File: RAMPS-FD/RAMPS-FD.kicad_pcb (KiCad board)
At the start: 2 copper layers, 100 x 100 mm, 171 parts, among them J1 NET-TIE, K201 S1, K202 S2, K203 S3, K204 S4, M101 LOGO_OSHW, P1 SERIAL1, P101 HB_IN, P102 RESET, P105 12V-AUX, P107 MOT_IN, P108 POWER_IN, P2 I2C-1, P201 3 2 1, P202 3 2 1, P203 3 2 1, P204 X, P205 Y, P206 Z1, P207 3 2 1, P208 3 2 1, P209 3 2 1, P210 E2, P211 I2C-0, P212 E1, P213 AUX-4, P214 AUX-2, P215 AUX-3, P216 SERIAL0, P217 E0, P218 D11, P219 EXT_5V, P3 Z2, P301 THERMISTORS, P302 ESTOP, P403 D9, P404 D8, P405 D10, P801 ENDSTOPS, P802 - X + - Y + - Z +, P901 D12, P902 D2, Q1 DMN2075, Q101 DMN2075, Q201 IRLB8743PBF, Q202 IRLB8743PBF, Q203 IRLB8743PBF, Q206 IRLB8743PBF, Q901 DMN2075U, Q902 DMN2075U, SW101 RESET, U1 74ACT125, U1001 TL431_SOT23_RMC, U2 74ACT244, U201 X, U202 Y, U203 Z, U204 E2, U205 E1, U206 E0, U3 LM7812, U4 L7805CV-DG, U601 24C512, U801 4050_RMC

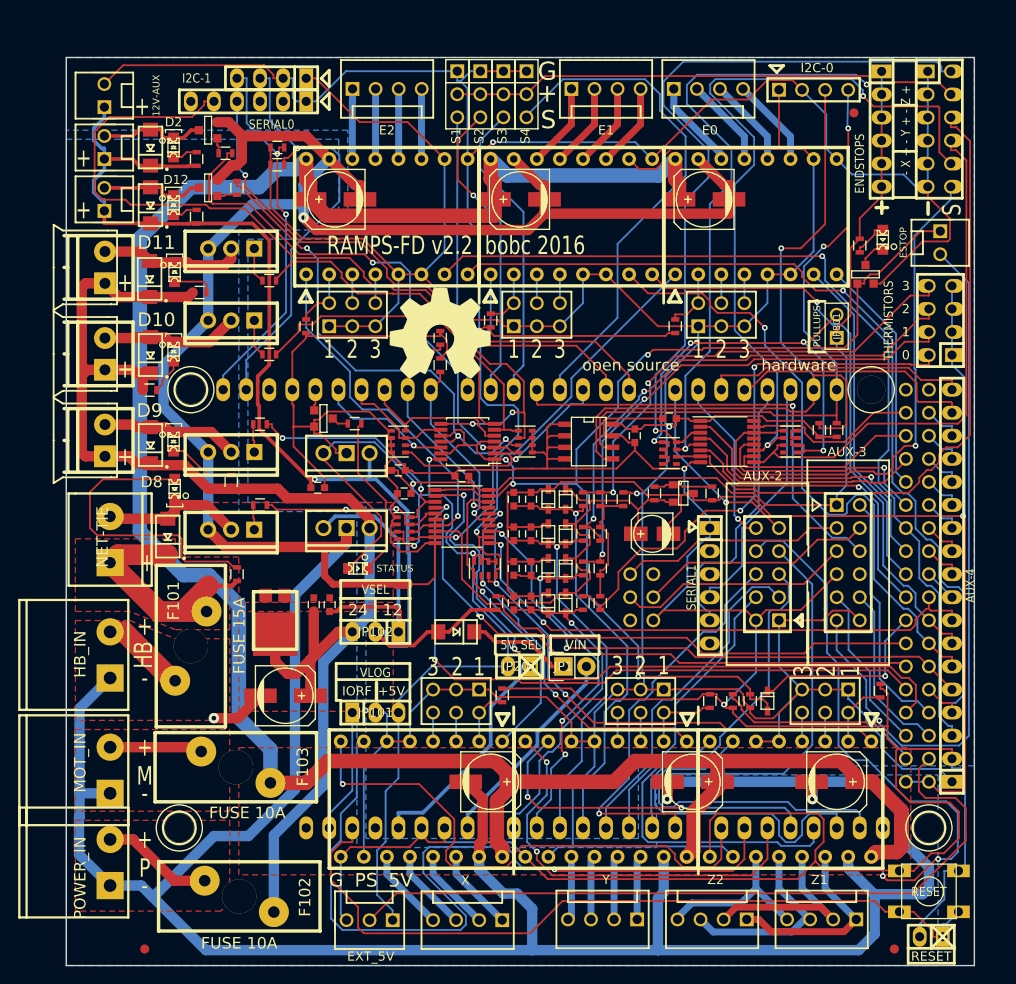
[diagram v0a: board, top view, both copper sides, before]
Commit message: Changed fuse holders to Keystone 3568; specificy HCT instead of ACT logic
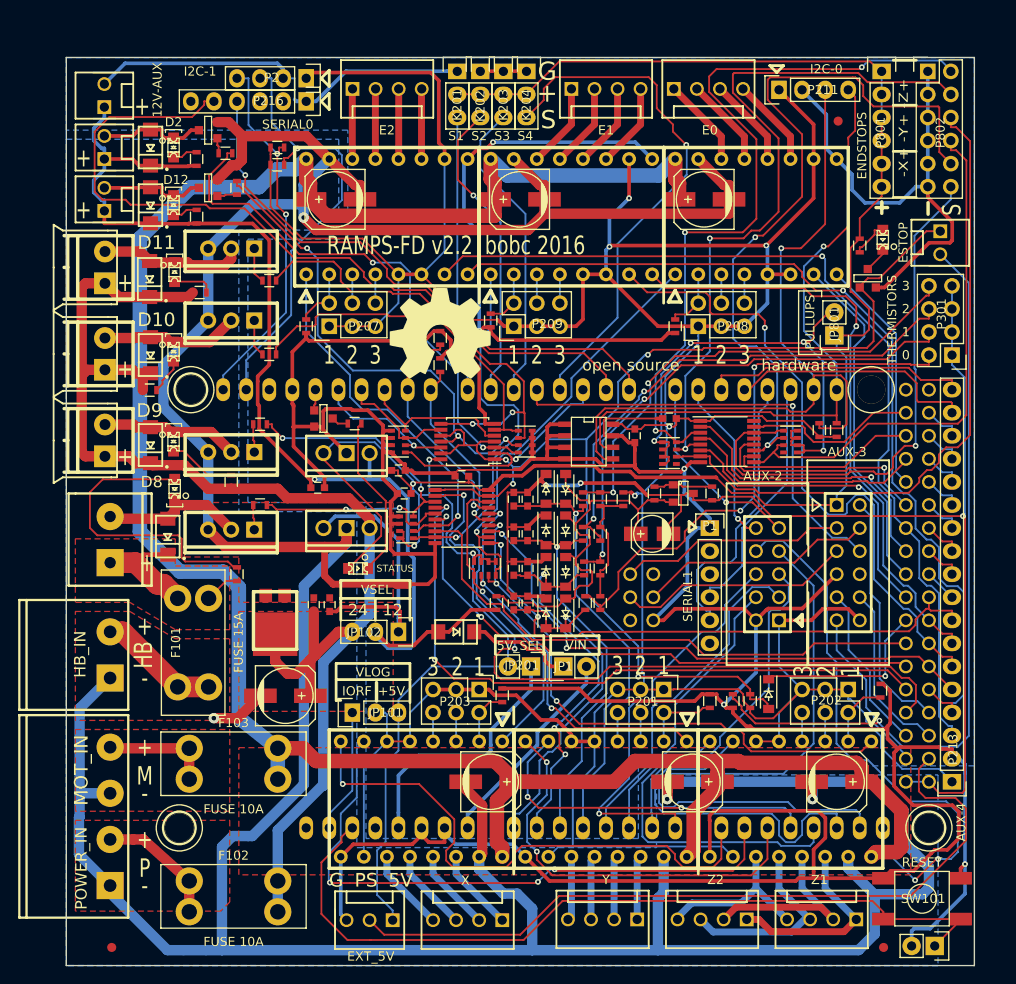
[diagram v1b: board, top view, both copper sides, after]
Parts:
- removed P107: MOT_IN, w_conn_screw:mstba_2,5%2f2-g-5,08
- C101: value 100u 35V -> 100u; 35V
- C102: value 100n 35V -> 100n; 50V
- C207, C3: value 100n 16V -> 100n
- D1001, D1002, D1003, D1004, D1005, D1006, D1007, D1008, D301: footprint w_smd_diode:SOD323 -> Diodes_SMD:SOD-123
- D102: value SS10Pxx -> V10P10
- F101, F102, F103: footprint rmc:FUSE-MINI-AUTO -> rmc:Keystone_3568
- JP101, JP102: footprint w_pin_strip:pin_strip_3 -> Pin_Headers:Pin_Header_Straight_1x03
- JP201, P102: footprint w_pin_strip:pin_strip_2 -> Pin_Headers:Pin_Header_Straight_1x02
- JP801: footprint pin_array:PIN_ARRAY_2X1 -> Pin_Headers:Pin_Header_Straight_1x02
- K201, K202, K203, K204: footprint pin_array:PIN_ARRAY_3X1 -> Pin_Headers:Pin_Header_Straight_1x03
- P1, P216, P801: footprint w_pin_strip:pin_strip_6 -> Pin_Headers:Pin_Header_Straight_1x06
- P108: footprint w_conn_screw:mstba_2,5%2f2-g-5,08 -> w_conn_screw:mstba_2,5%2f4-g-5,08
- P2: footprint w_pin_strip:pin_strip_4 -> Pin_Headers:Pin_Header_Straight_1x04
- P201, P202, P203, P207, P208, P209: footprint pin_array:pin_array_3x2 -> Pin_Headers:Pin_Header_Straight_2x03
- P211: footprint pin_array:PIN_ARRAY_4x1 -> Pin_Headers:Pin_Header_Straight_1x04
- P213: footprint w_pin_strip:pin_strip_18 -> Pin_Headers:Pin_Header_Straight_1x18
- P301: footprint w_pin_strip:pin_strip_4x2 -> Pin_Headers:Pin_Header_Straight_2x04
- P802: value - X + - Y + - Z + -> -X+ -Y+ -Z+; footprint w_pin_strip:pin_strip_6x2 -> Pin_Headers:Pin_Header_Straight_2x06
- SW101: footprint rmc:SW_6x6_MULTI -> rmc:SW_6x6_SMD
- U1: value 74ACT125 -> 74HCT125
- U2: value 74ACT244 -> 74HCT244
- U801: value 4050_RMC -> 74HC4050
- moved P213 21.6 mm to (149.9, 119.4), turned to 180 degrees
- moved P802 6.48 mm to (147.2, 41.1), turned to 0 degrees
- moved P1 6.35 mm to (123.2, 91.4), turned to 0 degrees
- moved P216 6.35 mm to (78.7, 44.5), turned to 270 degrees
- moved P801 6.35 mm to (142.1, 41.1), turned to 0 degrees
- moved P108 5.08 mm to (57.1, 123.2)
- moved P301 4.02 mm to (149.9, 72.4), turned to 180 degrees
- moved P211 3.81 mm to (130.8, 43.2), turned to 90 degrees
- moved P2 3.81 mm to (78.7, 41.9), turned to 270 degrees
- moved FID1 3.64 mm to (57.3, 137.6)
- moved P202 2.84 mm to (138.4, 109.2), turned to 270 degrees
- moved P209 2.84 mm to (101.6, 69.2), turned to 90 degrees
- moved P201 2.84 mm to (118.1, 109.2), turned to 270 degrees
- moved P203 2.84 mm to (97.8, 109.2), turned to 270 degrees
- moved P207 2.84 mm to (81.3, 69.2), turned to 90 degrees
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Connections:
- D103 pad 1: +12P -> /Power/LP_1
- D103 pad 2: /Power/LP_1 -> +12P
- D301 pad 1: Net-(D301-Pad1) -> ESTOP
- D301 pad 2: ESTOP -> Net-(D301-Pad2)
- D401 pad 1: /Mosfet Outputs/D9_OUT -> +V_POWER
- D401 pad 2: +V_POWER -> /Mosfet Outputs/D9_OUT
- D402 pad 1: /Mosfet Outputs/D10_OUT -> +V_POWER
- D402 pad 2: +V_POWER -> /Mosfet Outputs/D10_OUT
- D403 pad 1: /Mosfet Outputs/FET4_OUT -> +V_POWER
- D403 pad 2: +V_POWER -> /Mosfet Outputs/FET4_OUT
- D404 pad 1: /Mosfet Outputs/D8_OUT -> +V_HEATBED
- D404 pad 2: +V_HEATBED -> /Mosfet Outputs/D8_OUT
- D903 pad 1: /Extra MOSFETs/P_FET5 -> +12P
- D903 pad 2: +12P -> /Extra MOSFETs/P_FET5
- D904 pad 1: /Extra MOSFETs/P_FET6 -> +12P
- D904 pad 2: +12P -> /Extra MOSFETs/P_FET6
- P302 pad 1: Net-(D301-Pad1) -> Net-(D301-Pad2)
- Q1 pad G: Net-(D301-Pad1) -> Net-(D301-Pad2)
- R304 pad 2: Net-(D301-Pad1) -> Net-(D301-Pad2)
- U1 pad 1: Net-(D301-Pad1) -> Net-(D301-Pad2)
- U1 pad 10: Net-(D301-Pad1) -> Net-(D301-Pad2)
- U1 pad 13: Net-(D301-Pad1) -> Net-(D301-Pad2)
- U1 pad 4: Net-(D301-Pad1) -> Net-(D301-Pad2)
- U2 pad 1: Net-(D301-Pad1) -> Net-(D301-Pad2)
- U2 pad 19: Net-(D301-Pad1) -> Net-(D301-Pad2)
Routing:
- net Net-(D301-Pad2): track 0.00 -> 138.3 mm, vias 0 -> 4
- net Net-(D301-Pad1): track 134.4 -> 0.00 mm, vias 4 -> 0
- net GND: track 626.7 -> 605.7 mm, vias 5 -> 6
- net X_STEP: track 87.5 -> 67.5 mm, vias 1 -> 3
- net +V_LOGIC: track 403.1 -> 421.5 mm, vias 2 -> 5
- net +5V: track 268.1 -> 273.2 mm
- net THERM1: track 41.4 -> 45.7 mm
- net /RESET: track 85.7 -> 89.8 mm
- net X_EN: track 77.0 -> 81.0 mm
- net /Power/HB_IN: track 9.39 -> 13.4 mm
- net +V_HEATBED: track 26.9 -> 23.1 mm
- net OV_REF: track 42.2 -> 45.6 mm
- net THERM0: track 37.9 -> 41.3 mm
- net /Z_EN_BUF: track 60.8 -> 63.3 mm
- net D39: track 61.0 -> 63.3 mm
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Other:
- net class Default: clearance 0.2032 -> 0.1778
- net class low-power: clearance 0.2032 -> 0.1778
- rule trace_clearance: 0.2032 -> 0.1778
- board text added: "MOT_IN"

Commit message: Fix 3d view; remove faulty ADC protection
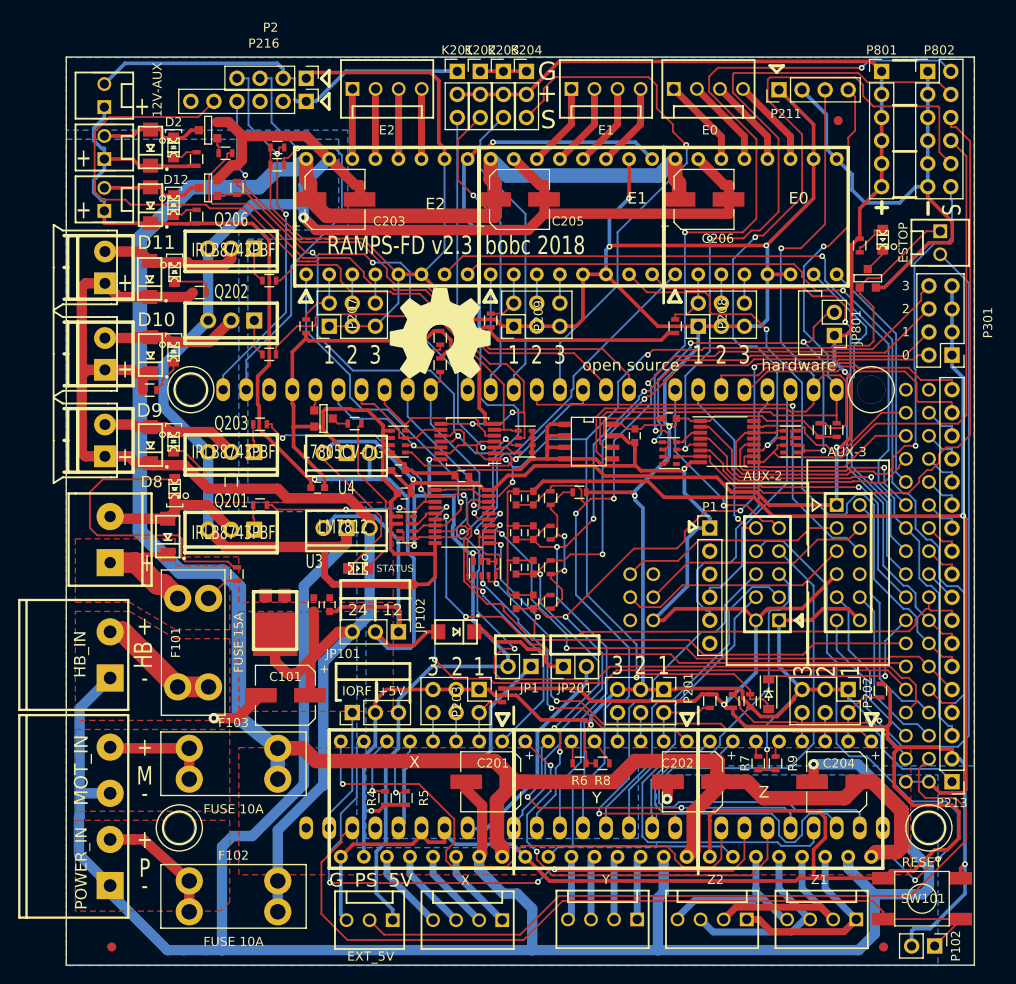
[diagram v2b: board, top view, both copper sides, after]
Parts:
- removed C1001: 10u, Capacitors_SMD:c_elec_4x5.3
- removed D1001, D1002, D1003, D1004, D1005, D1006, D1007, D1008: 1N4148, Diodes_SMD:SOD-123
- removed R1002: 6k8, Resistors_SMD:R_0603
- removed R1003: 1k8, Resistors_SMD:R_0603
- removed R1004: 1k, Resistors_SMD:R_0603
- removed R502, R503, R504, R505: 4k7, Resistors_SMD:R_0603
- removed U1001: TL431_SOT23_RMC, libcms:SOT23
- added R4: 10k, Resistors_SMD:R_0603, F.Cu at (87.4, 121.2)
- added R5: 10k, Resistors_SMD:R_0603, F.Cu at (89.7, 121.2)
- added R6: 10k, Resistors_SMD:R_0603, F.Cu at (108.8, 117.3)
- added R7: 10k, Resistors_SMD:R_0603, F.Cu at (128.5, 117.3)
- added R8: 10k, Resistors_SMD:R_0603, F.Cu at (111.4, 117.3)
- added R9: 10k, Resistors_SMD:R_0603, F.Cu at (130.4, 117.3)
- C101: value 100u; 35V -> 100u 35V; footprint Capacitors_SMD:c_elec_6.3x7.7 -> Capacitors_SMD:CP_Elec_6.3x7.7
- C102: value 100n; 50V -> 100n 50V
- C201, C202, C203, C204, C205, C206: footprint Capacitors_SMD:c_elec_6.3x7.7 -> Capacitors_SMD:CP_Elec_6.3x7.7
- JP1, JP201, JP801, P102: footprint Pin_Headers:Pin_Header_Straight_1x02 -> Pin_Headers:Pin_Header_Straight_1x02_Pitch2.54mm
- JP101, JP102, K201, K202, K203, K204: footprint Pin_Headers:Pin_Header_Straight_1x03 -> Pin_Headers:Pin_Header_Straight_1x03_Pitch2.54mm
- P1, P216, P801: footprint Pin_Headers:Pin_Header_Straight_1x06 -> Pin_Headers:Pin_Header_Straight_1x06_Pitch2.54mm
- P2, P211: footprint Pin_Headers:Pin_Header_Straight_1x04 -> Pin_Headers:Pin_Header_Straight_1x04_Pitch2.54mm
- P201, P202, P203, P207, P208, P209: footprint Pin_Headers:Pin_Header_Straight_2x03 -> Pin_Headers:Pin_Header_Straight_2x03_Pitch2.54mm
- P213: footprint Pin_Headers:Pin_Header_Straight_1x18 -> Pin_Headers:Pin_Header_Straight_1x18_Pitch2.54mm
- P301: footprint Pin_Headers:Pin_Header_Straight_2x04 -> Pin_Headers:Pin_Header_Straight_2x04_Pitch2.54mm
- P802: footprint Pin_Headers:Pin_Header_Straight_2x06 -> Pin_Headers:Pin_Header_Straight_2x06_Pitch2.54mm
- moved R301 5.46 mm to (105.7, 99.6), turned to 90 degrees
- moved R302 5.46 mm to (105.7, 95.8)
- moved R303 5.46 mm to (105.7, 91.9), turned to 90 degrees
- moved R501 5.46 mm to (105.7, 88.1)
- moved L1 4.89 mm to (108.8, 87.5), turned to 180 degrees
- moved C503 0.65 mm to (103.8, 91.9)
- moved C505 0.65 mm to (103.8, 95.8)
- moved C502 0.65 mm to (103.8, 88.1)
- moved C504 0.65 mm to (103.8, 99.6)
- moved J1 0.59 mm to (89.9, 97.7)
- moved C302 0.28 mm to (101.9, 95.8)
- moved C303 0.28 mm to (101.9, 91.9)
- moved C301 0.28 mm to (101.9, 99.6)
- moved C501 0.28 mm to (101.9, 88.1)
- moved FID2 0.05 mm to (137.3, 46.6)
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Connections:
- net Net-(P201-Pad6) renamed STEP_Y_CS
- net Net-(P202-Pad6) renamed STEP_Z_CS
- net Net-(P203-Pad6) renamed STEP_X_CS
- P301 pad 2: Net-(P301-Pad2) -> THERM0
- P301 pad 4: Net-(P301-Pad4) -> THERM1
- P301 pad 6: Net-(P301-Pad6) -> THERM2
- P301 pad 8: Net-(P301-Pad8) -> THERM3
- R301 pad 2: Net-(P301-Pad2) -> THERM0
- R302 pad 2: Net-(P301-Pad4) -> THERM1
- R303 pad 2: Net-(P301-Pad6) -> THERM2
- R501 pad 2: Net-(P301-Pad8) -> THERM3
- U201 pad 5: +V_LOGIC -> Net-(J3-Pad6)
- U201 pad 6: +V_LOGIC -> Net-(R4-Pad2)
- U202 pad 5: +V_LOGIC -> Net-(J5-Pad6)
- U202 pad 6: +V_LOGIC -> Net-(R6-Pad2)
- U203 pad 5: +V_LOGIC -> Net-(J4-Pad6)
- U203 pad 6: +V_LOGIC -> Net-(R7-Pad2)
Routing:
- net Net-(P301-Pad2): track 61.0 -> 0.00 mm, vias 2 -> 0
- net THERM0: track 41.3 -> 98.2 mm, vias 1 -> 3
- net Net-(P301-Pad4): track 56.7 -> 0.00 mm, vias 2 -> 0
- net THERM3: track 48.8 -> 105.4 mm, vias 1 -> 3
- net THERM2: track 43.3 -> 99.5 mm, vias 1 -> 3
- net Net-(P301-Pad6): track 56.2 -> 0.00 mm, vias 2 -> 0
- net Net-(P301-Pad8): track 53.1 -> 0.00 mm, vias 2 -> 0
- net THERM1: track 45.7 -> 98.6 mm, vias 3 -> 5
- net OV_REF: track 45.6 -> 0.00 mm
- net MOT_GND: track 447.2 -> 430.1 mm
- net +V_LOGIC: track 421.5 -> 436.7 mm, vias 5 -> 8
- net GNDA: track 148.4 -> 135.3 mm, vias 3 -> 1
- net Net-(R4-Pad2): track 0.00 -> 7.56 mm, vias 0 -> 1
- net Net-(J3-Pad6): track 0.00 -> 7.52 mm, vias 0 -> 1
- net +12P: track 126.7 -> 119.3 mm
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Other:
- board text added: "RAMPS-FD v2.3 bobc 2018"
- board text removed: "RAMPS-FD v2.2 bobc 2016"
